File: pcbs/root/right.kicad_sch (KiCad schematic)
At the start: 0 parts

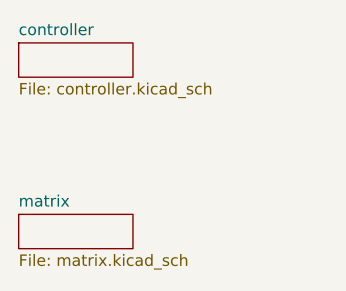
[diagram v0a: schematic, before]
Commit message: Assign the matrix J1 pins per side to match the routing
Order the J1 pins so each net leaves toward its destination (columns
C0-C3 on one side, C5-C6 on the other, rows above and below), mirrored
between the halves:
  left  (pin 11..1): C3 C2 C1 C0 R3 R2 R1 R0 C4 C6 C5
  right (pin 11..1): C5 C6 R3 R2 R1 R0 C4 C0 C1 C2 C3
The controller board and cable are unchanged; with matrix pin k on
controller pin 12 - k, the XIAO pins become
  left:  C0-C6 = D3 D4 D5 D6 D9 D7 D8, R0-R3 = D10 D0 D1 D2
  right: C0-C6 = D10 D9 D8 D7 D0 D6 D5, R0-R3 = D1 D2 D3 D4
Split the root project's shared matrix sheet into left and right copies.

Co-Authored-By: Claude Opus 5.5 <noreply@anthropic.com>
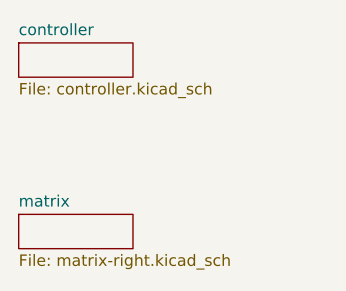
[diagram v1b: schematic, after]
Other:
- sheet matrix: file matrix.kicad_sch -> matrix-right.kicad_sch
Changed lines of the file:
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@@
 			)
 		)
-		(property "Sheetfile" "matrix.kicad_sch"
+		(property "Sheetfile" "matrix-right.kicad_sch"
 			(at 29.21 51.3846 0)
 			(show_name no)
